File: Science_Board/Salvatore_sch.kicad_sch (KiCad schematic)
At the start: 6 parts

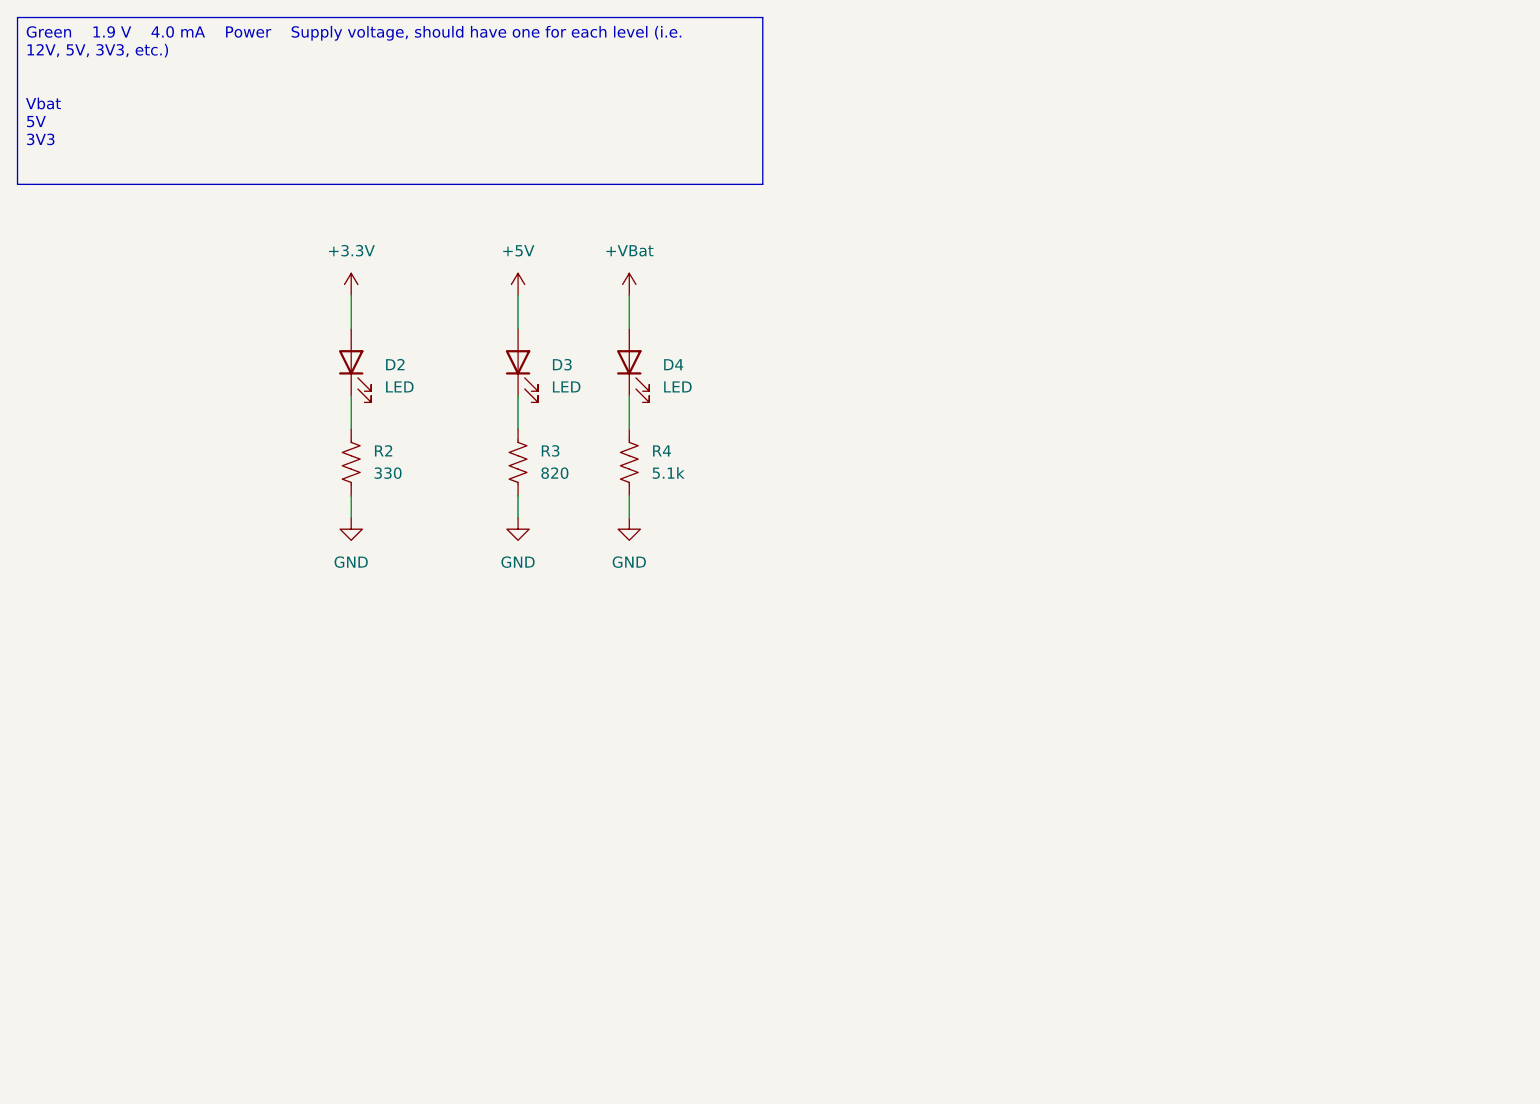
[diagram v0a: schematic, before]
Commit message: added the PWM driver
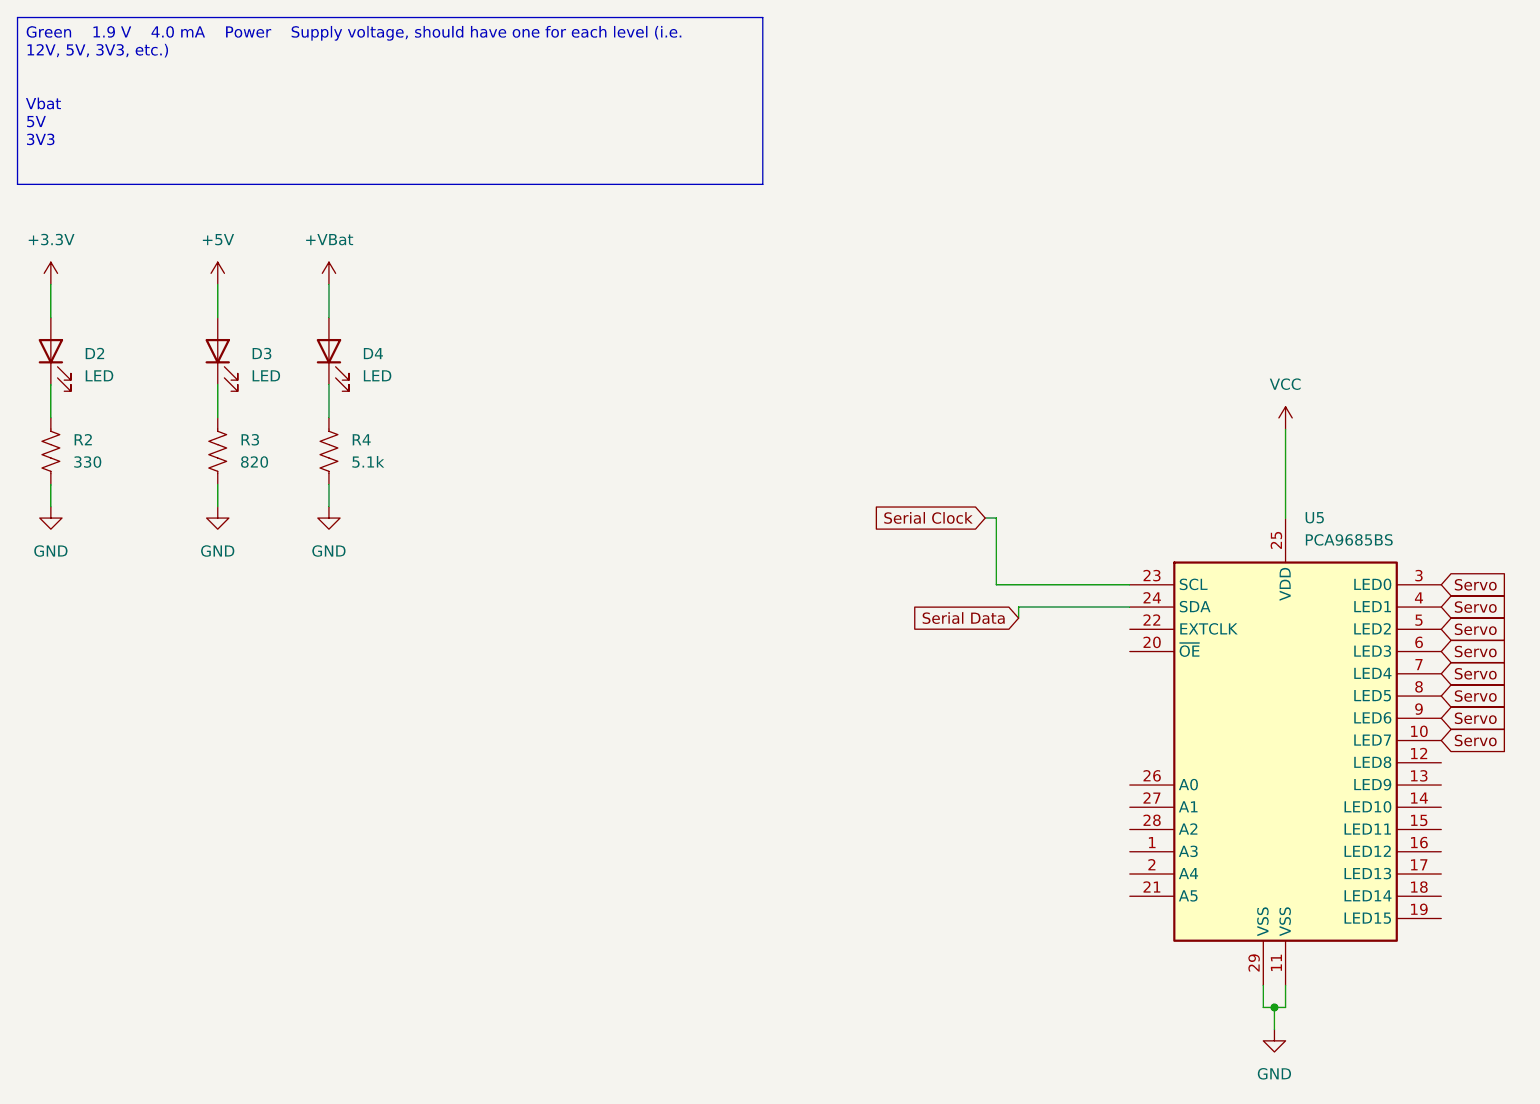
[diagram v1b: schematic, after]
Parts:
- added U5: PCA9685BS, Package_DFN_QFN:QFN-28-1EP_6x6mm_P0.65mm_EP4.25x4.25mm, symbol Driver_LED:PCA9685BS
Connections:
- net GND: now also U5.11 (VSS), U5.29 (VSS)
- new net Serial Clock: U5.23 (SCL)
- new net Serial Data: U5.24 (SDA)
- new net Servo: U5.10 (LED7), U5.3 (LED0), U5.4 (LED1), U5.5 (LED2), U5.6 (LED3), U5.7 (LED4), U5.8 (LED5), U5.9 (LED6)
- new net VCC: U5.25 (VDD)
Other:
- moved on the sheet: D2, D3, D4, R2, R3, R4
